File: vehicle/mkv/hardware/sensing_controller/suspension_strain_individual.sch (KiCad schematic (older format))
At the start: 9 parts, among them U601 MCP6001T-I-LT

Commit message: Fix silkscreen on Sensing Controller. (#58)
* Increase power plane size.

Increase the size of the 5.5V and 3.3V power planes.

* Add test points.

Add test points for PM/SM Miso/Mosi/CS.

* Add front/left sense test points.

* Make silkscreen legible.

* Remove rescue lib

* Remove Gerber zip file from output

* Buildifer

Co-authored-by: Jack Greenberg <j@jackgreenberg.co>
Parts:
- C601: symbol sensing_controller-rescue:C_0.1uF-formula -> formula:C_0.1uF
- R601, R603, R604, R605, R606: symbol sensing_controller-rescue:R_120-formula -> formula:R_120
- R602, R607: symbol sensing_controller-rescue:R_4.99K-formula -> formula:R_4.99K
- U601: symbol sensing_controller-rescue:MCP6001T-I-LT-formula -> formula:MCP6001T-I-LT
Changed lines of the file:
@@
 $Descr B 17000 11000
 encoding utf-8
-Sheet 6 20
+Sheet 15 20
 Title "Strain Gauge Circuit"
 Date "2021-05-22"
@@
 $EndDescr
 $Comp
-L sensing_controller-rescue:R_120-formula R603
+L formula:R_120 R603
 U 1 1 60AD0DF7
 P 5800 4950
@@
 AR Path="/60A3D9FD/60ABA307/60AD0DF7" Ref="R1603"  Part="1"
 AR Path="/60A3D9FD/60ABA487/60AD0DF7" Ref="R1703"  Part="1"
-F 0 "R603" H 5730 4904 50  0000 R CNN
+F 0 "R1503" H 5730 4904 50  0000 R CNN
 F 1 "R_120" H 5730 4995 50  0000 R CNN
 F 2 "footprints:R_0805_OEM" H 4600 5100 50  0001 L CNN
@@
 $EndComp
 $Comp
-L sensing_controller-rescue:R_120-formula R605
+L formula:R_120 R605
 U 1 1 60AD1909
 P 5800 5450
@@
 AR Path="/60A3D9FD/60ABA307/60AD1909" Ref="R1605"  Part="1"
 AR Path="/60A3D9FD/60ABA487/60AD1909" Ref="R1705"  Part="1"
-F 0 "R605" H 5730 5404 50  0000 R CNN
+F 0 "R1505" H 5730 5404 50  0000 R CNN
 F 1 "R_120" H 5730 5495 50  0000 R CNN
 F 2 "footprints:R_0805_OEM" H 4600 5600 50  0001 L CNN
@@
 $EndComp
 $Comp
-L sensing_controller-rescue:R_120-formula R604
+L formula:R_120 R604
 U 1 1 60AD1D1E
 P 6650 4950
@@
 AR Path="/60A3D9FD/60ABA307/60AD1D1E" Ref="R1604"  Part="1"
 AR Path="/60A3D9FD/60ABA487/60AD1D1E" Ref="R1704"  Part="1"
-F 0 "R604" H 6580 4904 50  0000 R CNN
+F 0 "R1504" H 6580 4904 50  0000 R CNN
 F 1 "R_120" H 6580 4995 50  0000 R CNN
 F 2 "footprints:R_0805_OEM" H 5450 5100 50  0001 L CNN
@@
 Amplification
 $Comp
-L sensing_controller-rescue:MCP6001T-I-LT-formula U601
+L formula:MCP6001T-I-LT U601
 U 1 1 60A9D27A
 P 9700 5050
@@
 AR Path="/60A3D9FD/60ABA307/60A9D27A" Ref="U1601"  Part="1"
 AR Path="/60A3D9FD/60ABA487/60A9D27A" Ref="U1701"  Part="1"
-F 0 "U601" H 9800 4900 50  0000 L CNN
+F 0 "U1501" H 9800 4900 50  0000 L CNN
 F 1 "MCP6001T-I-LT" H 9800 5150 50  0000 L CNN
 F 2 "Package_TO_SOT_SMD:SOT-353_SC-70-5" H 9600 5150 50  0001 C CNN
@@
 	9600 4500 9600 4600
 $Comp
-L sensing_controller-rescue:C_0.1uF-formula C601
+L formula:C_0.1uF C601
 U 1 1 60A9EBA8
 P 9900 4600
@@
 AR Path="/60A3D9FD/60ABA307/60A9EBA8" Ref="C1601"  Part="1"
 AR Path="/60A3D9FD/60ABA487/60A9EBA8" Ref="C1701"  Part="1"
-F 0 "C601" V 9648 4600 50  0000 C CNN
+F 0 "C1501" V 9648 4600 50  0000 C CNN
 F 1 "C_0.1uF" V 9739 4600 50  0000 C CNN
 F 2 "footprints:C_0805_OEM" H 9938 4450 50  0001 C CNN
@@
 WHEATSTONE_OUT_-
 $Comp
-L sensing_controller-rescue:R_120-formula R601
+L formula:R_120 R601
 U 1 1 60AA43F4
 P 8650 4450
@@
 AR Path="/60A3D9FD/60ABA307/60AA43F4" Ref="R1601"  Part="1"
 AR Path="/60A3D9FD/60ABA487/60AA43F4" Ref="R1701"  Part="1"
-F 0 "R601" V 8443 4450 50  0000 C CNN
+F 0 "R1501" V 8443 4450 50  0000 C CNN
 F 1 "R_120" V 8534 4450 50  0000 C CNN
 F 2 "footprints:R_0805_OEM" H 7450 4600 50  0001 L CNN
@@
 $EndComp
 $Comp
-L sensing_controller-rescue:R_120-formula R606
+L formula:R_120 R606
 U 1 1 60AA4A94
 P 8650 5700
@@
 AR Path="/60A3D9FD/60ABA307/60AA4A94" Ref="R1606"  Part="1"
 AR Path="/60A3D9FD/60ABA487/60AA4A94" Ref="R1706"  Part="1"
-F 0 "R606" V 8550 5700 50  0000 C CNN
+F 0 "R1506" V 8550 5700 50  0000 C CNN
 F 1 "R_120" V 8450 5700 50  0000 C CNN
 F 2 "footprints:R_0805_OEM" H 7450 5850 50  0001 L CNN
@@
 $EndComp
 $Comp
-L sensing_controller-rescue:R_4.99K-formula R607
+L formula:R_4.99K R607
 U 1 1 60AA8E34
 P 9450 5700
@@
 AR Path="/60A3D9FD/60ABA307/60AA8E34" Ref="R1607"  Part="1"
 AR Path="/60A3D9FD/60ABA487/60AA8E34" Ref="R1707"  Part="1"
-F 0 "R607" V 9350 5700 50  0000 C CNN
+F 0 "R1507" V 9350 5700 50  0000 C CNN
 F 1 "R_4.99K" V 9250 5700 50  0000 C CNN
 F 2 "footprints:R_0805_OEM" H 9250 5650 50  0001 C CNN
@@
 	9300 4450 9300 4950
 $Comp
-L sensing_controller-rescue:R_4.99K-formula R602
+L formula:R_4.99K R602
 U 1 1 60AAF6BB
 P 8900 4700
@@
 AR Path="/60A3D9FD/60ABA307/60AAF6BB" Ref="R1602"  Part="1"
 AR Path="/60A3D9FD/60ABA487/60AAF6BB" Ref="R1702"  Part="1"
-F 0 "R602" H 8830 4654 50  0000 R CNN
+F 0 "R1502" H 8830 4654 50  0000 R CNN
 F 1 "R_4.99K" H 8830 4745 50  0000 R CNN
 F 2 "footprints:R_0805_OEM" H 8700 4650 50  0001 C CNN

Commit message: Add new inAmp for strain gauge.
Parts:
- removed R603, R604, R605: R_120, footprints:R_0805_OEM, symbol formula:R_120
- added C1: C_1uF, footprints:C_0805_OEM, symbol formula:C_1uF
- added C2: C_100pF, footprints:C_0805_OEM, symbol formula:C_100pF
- added R3: R_100, footprints:R_0805_OEM, symbol formula:R_100
- added R4: R_1.18M, footprints:R_0805_OEM, symbol formula:R_1.18M
- added R?: R_120_05, footprints:R_0805_OEM, symbol formula:R_120_05
- added R?: R_3.92k, footprints:R_0805_OEM, symbol formula:R_3.92k
- added U1: AD8553ARMZ-REEL, RM_10_ADI, symbol formula:AD8553ARMZ-REEL
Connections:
- wire segments 38 -> 54
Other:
- note added: "Amplification Gain = 2* (1.18M/4k) = 590"
- note added: "Traces from Pin 1 and Pin 10 to R_ should be kept short and symmetric to minimize parasitic capacitance"
- moved on the sheet: C601, U601

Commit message: Add buffers for voltage references.
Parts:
- removed C601: C_0.1uF, footprints:C_0805_OEM, symbol formula:C_0.1uF
- removed R601, R606: R_120, footprints:R_0805_OEM, symbol formula:R_120
- removed R602, R607: R_4.99K, footprints:R_0805_OEM, symbol formula:R_4.99K
- removed U601: MCP6001T-I-LT, Package_TO_SOT_SMD:SOT-353_SC-70-5, symbol formula:MCP6001T-I-LT
- gave numbers to parts that had none: 2
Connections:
- net labels added: STRAIN_VOLTAGE_REF_2INAMP
- wire segments 54 -> 30
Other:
- note added: "Traces from Pin 1 and Pin 10 to R_14\nshould be kept short and symmetric \nto minimize parasitic capacitance"
- note removed: "Amplification"
- note removed: "Amplification gain (based on confluence): 71.5k/120 = 595.833"
- note removed: "Rg should be 71.5k"
- note removed: "TODO: Revisit the amplification resistors based on the confluence page and Lucky’s documentation\nhttps://docs.google.com/document/d/1uiaLruZ--4WWROcz7pXYCfJ-SIK90jK-znLseS2YlBg/edit#\nhttps://docs.olinelectricmotorsports.com/display/MD/Suspension+Strain"
- note removed: "Traces from Pin 1 and Pin 10 to R_ should be kept short and symmetric to minimize parasitic capacitance"

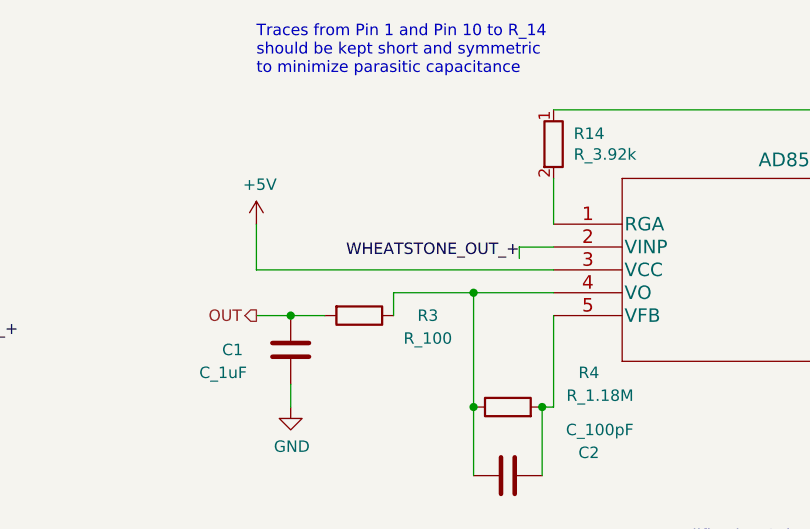
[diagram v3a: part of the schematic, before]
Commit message: Get rid of rescue parts.
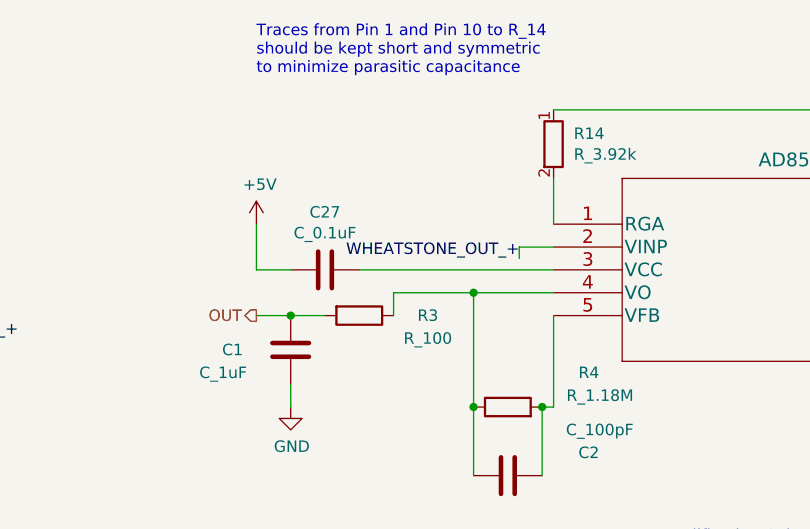
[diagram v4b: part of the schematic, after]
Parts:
- added C27: C_0.1uF, footprints:C_0805_OEM, symbol formula:C_0.1uF
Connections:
- net +5V: now also C27.2; no longer U1.3 (VCC)
- new net: C27.1, U1.3 (VCC)
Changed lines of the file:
@@
 $EndComp
 Wire Wire Line
-	6900 5000 5600 5000
+	6900 5000 6050 5000
 Wire Wire Line
 	5600 4800 5600 5000
@@
 Text GLabel 9600 5100 2    50   Input ~ 0
 STRAIN_VOLTAGE_REF_2INAMP
+$Comp
+L formula:C_0.1uF C27
+U 1 1 619539F1
+P 5900 5000
+AR Path="/60A3D9FD/60AD06C7/619539F1" Ref="C27"  Part="1"
+AR Path="/60A3D9FD/60AB905F/619539F1" Ref="C28"  Part="1"
+AR Path="/60A3D9FD/60AB9387/619539F1" Ref="C29"  Part="1"
+AR Path="/60A3D9FD/60AB9617/619539F1" Ref="C30"  Part="1"
+AR Path="/60A3D9FD/60AB9863/619539F1" Ref="C31"  Part="1"
+AR Path="/60A3D9FD/60AB9A43/619539F1" Ref="C32"  Part="1"
+AR Path="/60A3D9FD/60ABA183/619539F1" Ref="C33"  Part="1"
+AR Path="/60A3D9FD/60ABA307/619539F1" Ref="C34"  Part="1"
+AR Path="/60A3D9FD/60ABA487/619539F1" Ref="C35"  Part="1"
+AR Path="/60A3D9FD/60AB9FB3/619539F1" Ref="C36"  Part="1"
+AR Path="/60A3D9FD/60AB9E33/619539F1" Ref="C37"  Part="1"
+AR Path="/60A3D9FD/60AB9C37/619539F1" Ref="C38"  Part="1"
+F 0 "C27" V 5648 5000 50  0000 C CNN
+F 1 "C_0.1uF" V 5739 5000 50  0000 C CNN
+F 2 "footprints:C_0805_OEM" H 5938 4850 50  0001 C CNN
+F 3 "http://datasheets.avx.com/X7RDielectric.pdf" H 5925 5100 50  0001 C CNN
+F 4 "DK" H 5900 5000 60  0001 C CNN "MFN"
+F 5 "478-3352-1-ND" H 5900 5000 60  0001 C CNN "MPN"
+F 6 "https://www.digikey.com/products/en?keywords=478-3352-1-ND" H 6325 5500 60  0001 C CNN "PurchasingLink"
+	1    5900 5000
+	0    1    1    0
+$EndComp
+Wire Wire Line
+	5750 5000 5600 5000
 $EndSCHEMATC

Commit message: Add missing parts and do strain gauge layout.
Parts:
- U1: footprint RM_10_ADI -> footprints:AD8553ARMZ-REEL
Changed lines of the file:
@@
 F 0 "U1" H 8200 5187 60  0000 C CNN
 F 1 "AD8553ARMZ-REEL" H 8200 5081 60  0000 C CNN
-F 2 "RM_10_ADI" H 8200 5040 60  0001 C CNN
+F 2 "footprints:AD8553ARMZ-REEL" H 8200 5040 60  0001 C CNN
 F 3 "https://www.analog.com/media/en/technical-documentation/data-sheets/AD8553.pdf" H 6900 4800 60  0001 C CNN
 F 4 "https://www.digikey.com/en/products/detail/analog-devices-inc/AD8553ARMZ-REEL/995767" H 6900 4800 50  0001 C CNN "PurchasingLink:"

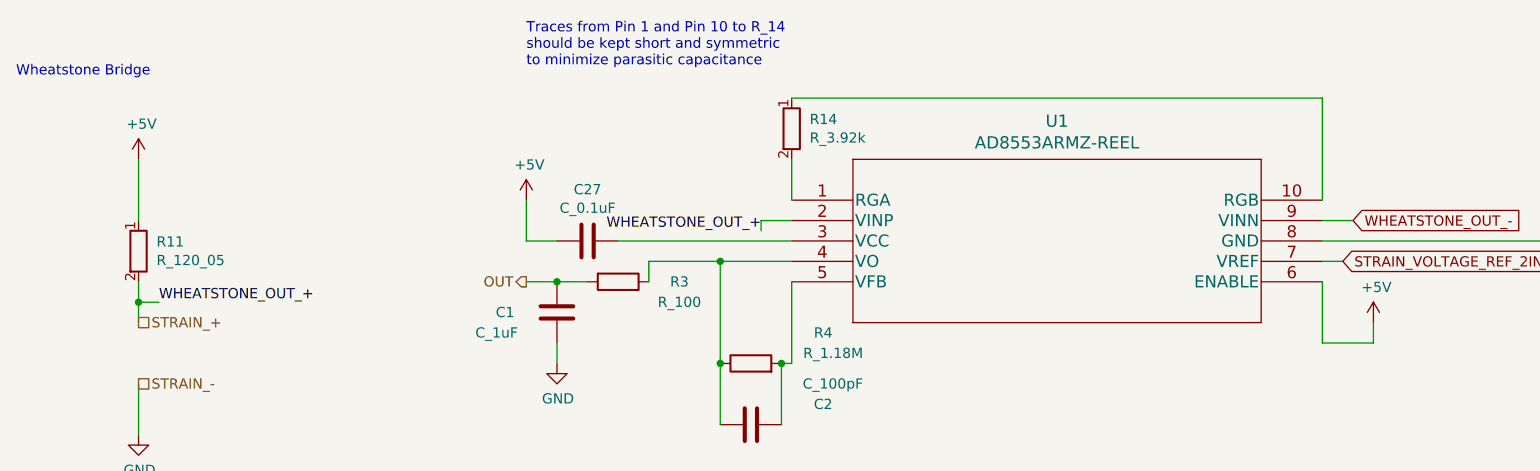
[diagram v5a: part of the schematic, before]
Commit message: Create functional blocks for sensing layout.
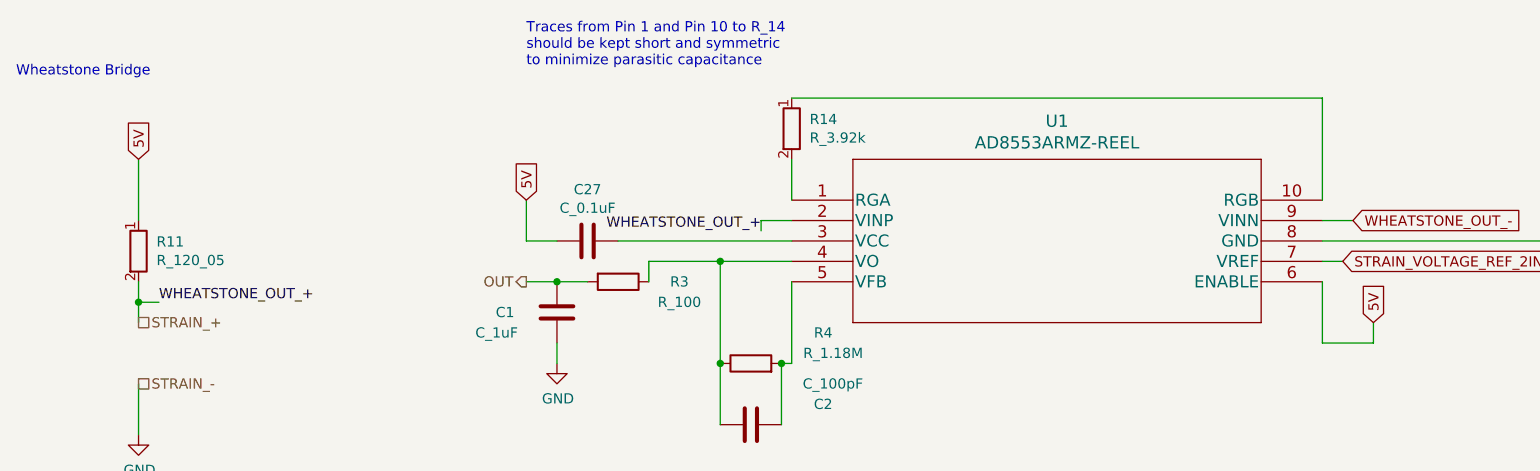
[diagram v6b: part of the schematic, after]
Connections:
- net +5V renamed 5V
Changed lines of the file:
@@
-	1    0    0    -1
-$EndComp
-$Comp
-L power:+5V #PWR?
-U 1 1 60AD370D
-P 3700 4600
-AR Path="/60A3D9FD/60AD06C7/60AD370D" Ref="#PWR?"  Part="1"
-AR Path="/60A3D9FD/60AB905F/60AD370D" Ref="#PWR?"  Part="1"
-AR Path="/60A3D9FD/60AB9387/60AD370D" Ref="#PWR?"  Part="1"
-AR Path="/60A3D9FD/60AB9617/60AD370D" Ref="#PWR?"  Part="1"
-AR Path="/60A3D9FD/60AB9863/60AD370D" Ref="#PWR?"  Part="1"
-AR Path="/60A3D9FD/60AB9A43/60AD370D" Ref="#PWR?"  Part="1"
-AR Path="/60A3D9FD/60AB9C37/60AD370D" Ref="#PWR?"  Part="1"
-AR Path="/60A3D9FD/60AB9E33/60AD370D" Ref="#PWR?"  Part="1"
-AR Path="/60A3D9FD/60AB9FB3/60AD370D" Ref="#PWR?"  Part="1"
-AR Path="/60A3D9FD/60ABA183/60AD370D" Ref="#PWR?"  Part="1"
-AR Path="/60A3D9FD/60ABA307/60AD370D" Ref="#PWR?"  Part="1"
-AR Path="/60A3D9FD/60ABA487/60AD370D" Ref="#PWR?"  Part="1"
-F 0 "#PWR?" H 3700 4450 50  0001 C CNN
-F 1 "+5V" H 3715 4773 50  0000 C CNN
-F 2 "" H 3700 4600 50  0001 C CNN
-F 3 "" H 3700 4600 50  0001 C CNN
-	1    3700 4600
 	1    0    0    -1
 $EndComp
@@
 Wire Wire Line
 	10900 5000 10900 5300
-$Comp
-L power:+5V #PWR?
-U 1 1 618B852B
-P 5600 4800
-AR Path="/60A3D9FD/60AD06C7/618B852B" Ref="#PWR?"  Part="1"
-AR Path="/60A3D9FD/60AB905F/618B852B" Ref="#PWR?"  Part="1"
-AR Path="/60A3D9FD/60AB9387/618B852B" Ref="#PWR?"  Part="1"
-AR Path="/60A3D9FD/60AB9617/618B852B" Ref="#PWR?"  Part="1"
-AR Path="/60A3D9FD/60AB9863/618B852B" Ref="#PWR?"  Part="1"
-AR Path="/60A3D9FD/60AB9A43/618B852B" Ref="#PWR?"  Part="1"
-AR Path="/60A3D9FD/60AB9C37/618B852B" Ref="#PWR?"  Part="1"
-AR Path="/60A3D9FD/60AB9E33/618B852B" Ref="#PWR?"  Part="1"
-AR Path="/60A3D9FD/60AB9FB3/618B852B" Ref="#PWR?"  Part="1"
-AR Path="/60A3D9FD/60ABA183/618B852B" Ref="#PWR?"  Part="1"
-AR Path="/60A3D9FD/60ABA307/618B852B" Ref="#PWR?"  Part="1"
-AR Path="/60A3D9FD/60ABA487/618B852B" Ref="#PWR?"  Part="1"
-F 0 "#PWR?" H 5600 4650 50  0001 C CNN
-F 1 "+5V" H 5615 4973 50  0000 C CNN
-F 2 "" H 5600 4800 50  0001 C CNN
-F 3 "" H 5600 4800 50  0001 C CNN
-	1    5600 4800
-	1    0    0    -1
-$EndComp
 Wire Wire Line
 	6900 5000 6050 5000
@@
 Wire Wire Line
 	9750 5400 9750 5500
-$Comp
-L power:+5V #PWR?
-U 1 1 618BB6B3
-P 9750 5400
-AR Path="/60A3D9FD/60AD06C7/618BB6B3" Ref="#PWR?"  Part="1"
-AR Path="/60A3D9FD/60AB905F/618BB6B3" Ref="#PWR?"  Part="1"
-AR Path="/60A3D9FD/60AB9387/618BB6B3" Ref="#PWR?"  Part="1"
-AR Path="/60A3D9FD/60AB9617/618BB6B3" Ref="#PWR?"  Part="1"
-AR Path="/60A3D9FD/60AB9863/618BB6B3" Ref="#PWR?"  Part="1"
-AR Path="/60A3D9FD/60AB9A43/618BB6B3" Ref="#PWR?"  Part="1"
-AR Path="/60A3D9FD/60AB9C37/618BB6B3" Ref="#PWR?"  Part="1"
-AR Path="/60A3D9FD/60AB9E33/618BB6B3" Ref="#PWR?"  Part="1"
-AR Path="/60A3D9FD/60AB9FB3/618BB6B3" Ref="#PWR?"  Part="1"
-AR Path="/60A3D9FD/60ABA183/618BB6B3" Ref="#PWR?"  Part="1"
-AR Path="/60A3D9FD/60ABA307/618BB6B3" Ref="#PWR?"  Part="1"
-AR Path="/60A3D9FD/60ABA487/618BB6B3" Ref="#PWR?"  Part="1"
-F 0 "#PWR?" H 9750 5250 50  0001 C CNN
-F 1 "+5V" H 9765 5573 50  0000 C CNN
-F 2 "" H 9750 5400 50  0001 C CNN
-F 3 "" H 9750 5400 50  0001 C CNN
-	1    9750 5400
-	1    0    0    -1
-$EndComp
 Text HLabel 5600 5200 0    50   Output ~ 0
 OUT
@@
 Wire Wire Line
 	5750 5000 5600 5000
+Text GLabel 3700 4600 1    50   Input ~ 0
+5V
+Text GLabel 5600 4800 1    50   Input ~ 0
+5V
+Text GLabel 9750 5400 1    50   Input ~ 0
+5V
 $EndSCHEMATC
